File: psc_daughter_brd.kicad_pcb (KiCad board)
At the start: 2 copper layers, 30.5 x 121.9 mm, 10 parts, among them U1 AD797, U4 AD5791xRUZ, U5 BUF634AxD

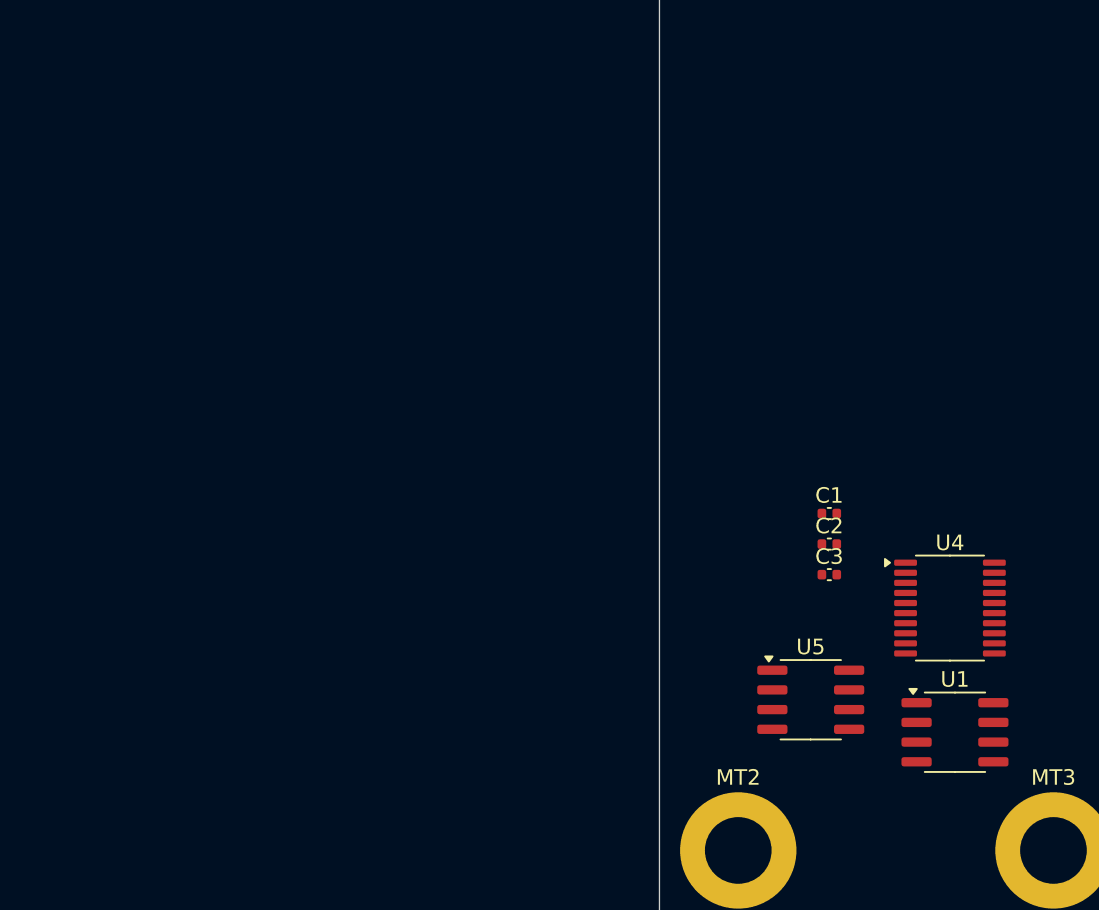
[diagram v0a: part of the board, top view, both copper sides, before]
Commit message: Add ADR1001 Voltage Reference
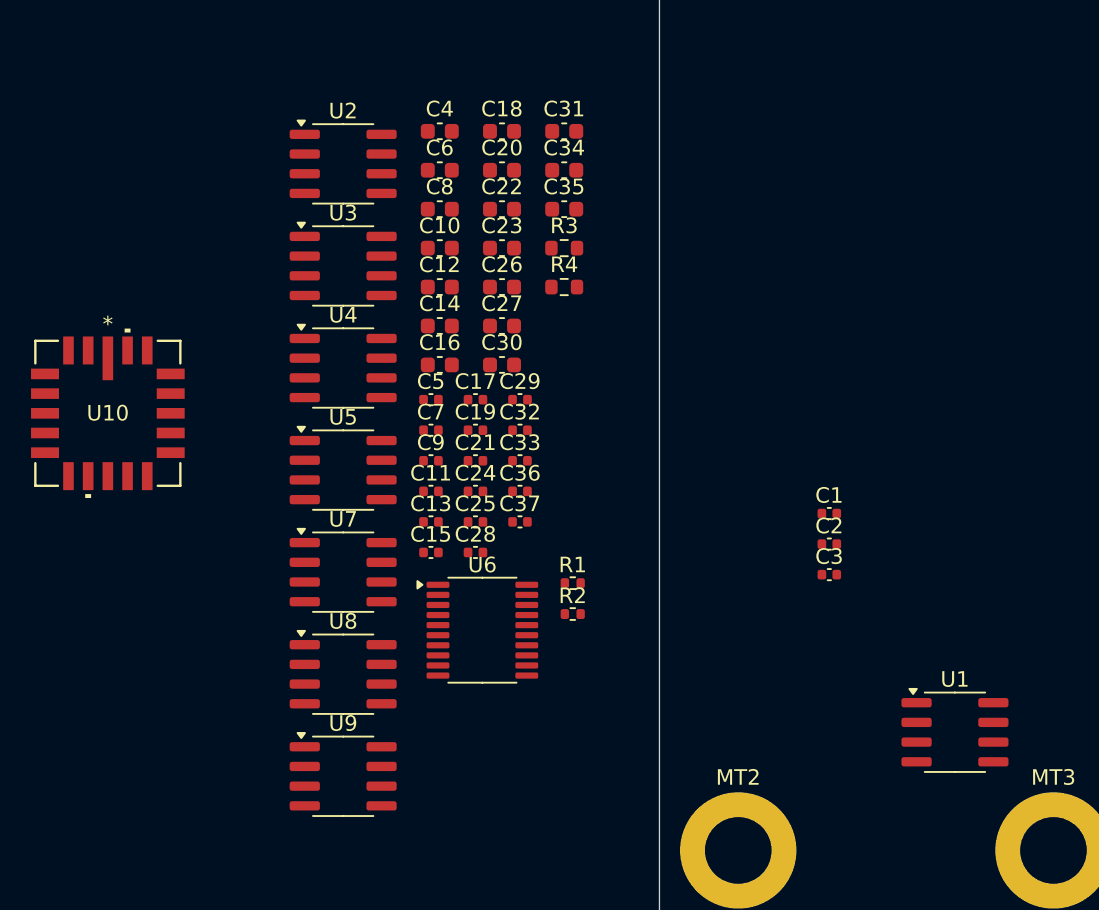
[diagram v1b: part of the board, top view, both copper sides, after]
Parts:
- added C10: 10uF, Capacitor_SMD:C_0603_1608Metric, F.Cu at (125.5, 147.9)
- added C11: 0.1uF, Capacitor_SMD:C_0402_1005Metric, F.Cu at (125.0, 163.5)
- added C12: 10uF, Capacitor_SMD:C_0603_1608Metric, F.Cu at (125.5, 150.4)
- added C13: 0.1uF, Capacitor_SMD:C_0402_1005Metric, F.Cu at (125.0, 165.5)
- added C14: 10uF, Capacitor_SMD:C_0603_1608Metric, F.Cu at (125.5, 152.9)
- added C15: 0.1uF, Capacitor_SMD:C_0402_1005Metric, F.Cu at (125.0, 167.5)
- added C16: 10uF, Capacitor_SMD:C_0603_1608Metric, F.Cu at (125.5, 155.4)
- added C17: 0.1uF, Capacitor_SMD:C_0402_1005Metric, F.Cu at (127.8, 157.6)
- added C18: 10uF, Capacitor_SMD:C_0603_1608Metric, F.Cu at (129.6, 140.3)
- added C19: 0.1uF, Capacitor_SMD:C_0402_1005Metric, F.Cu at (127.8, 159.6)
- added C20: 10uF, Capacitor_SMD:C_0603_1608Metric, F.Cu at (129.6, 142.8)
- added C21: 0.1uF, Capacitor_SMD:C_0402_1005Metric, F.Cu at (127.8, 161.6)
- added C22: 10uF, Capacitor_SMD:C_0603_1608Metric, F.Cu at (129.6, 145.3)
- added C23: 10uF, Capacitor_SMD:C_0603_1608Metric, F.Cu at (129.6, 147.9)
- added C24: 0.1uF, Capacitor_SMD:C_0402_1005Metric, F.Cu at (127.8, 163.5)
- added C25: 0.1uF, Capacitor_SMD:C_0402_1005Metric, F.Cu at (127.8, 165.5)
- added C26: 10uF, Capacitor_SMD:C_0603_1608Metric, F.Cu at (129.6, 150.4)
- added C27: 10uF, Capacitor_SMD:C_0603_1608Metric, F.Cu at (129.6, 152.9)
- added C28: 0.1uF, Capacitor_SMD:C_0402_1005Metric, F.Cu at (127.8, 167.5)
- added C29: 0.1uF, Capacitor_SMD:C_0402_1005Metric, F.Cu at (130.7, 157.6)
- added C30: 10uF, Capacitor_SMD:C_0603_1608Metric, F.Cu at (129.6, 155.4)
- added C31: 10uF, Capacitor_SMD:C_0603_1608Metric, F.Cu at (133.6, 140.3)
- added C32: 0.1uF, Capacitor_SMD:C_0402_1005Metric, F.Cu at (130.7, 159.6)
- added C33: 0.1uF, Capacitor_SMD:C_0402_1005Metric, F.Cu at (130.7, 161.6)
- added C34: 10uF, Capacitor_SMD:C_0603_1608Metric, F.Cu at (133.6, 142.8)
- added C35: 10uF, Capacitor_SMD:C_0603_1608Metric, F.Cu at (133.6, 145.3)
- added C36: 0.1uF, Capacitor_SMD:C_0402_1005Metric, F.Cu at (130.7, 163.5)
- added C37: 0.1uF, Capacitor_SMD:C_0402_1005Metric, F.Cu at (130.7, 165.5)
- added C4: 10uF, Capacitor_SMD:C_0603_1608Metric, F.Cu at (125.5, 140.3)
- added C5: 0.1uF, Capacitor_SMD:C_0402_1005Metric, F.Cu at (125.0, 157.6)
- added C6: 10uF, Capacitor_SMD:C_0603_1608Metric, F.Cu at (125.5, 142.8)
- added C7: 0.1uF, Capacitor_SMD:C_0402_1005Metric, F.Cu at (125.0, 159.6)
- added C8: 10uF, Capacitor_SMD:C_0603_1608Metric, F.Cu at (125.5, 145.3)
- added C9: 0.1uF, Capacitor_SMD:C_0402_1005Metric, F.Cu at (125.0, 161.6)
- added R1: 5.11K, Resistor_SMD:R_0402_1005Metric, F.Cu at (134.1, 169.5)
- added R2: 5.11K, Resistor_SMD:R_0402_1005Metric, F.Cu at (134.1, 171.4)
- added R3: 100, Resistor_SMD:R_0603_1608Metric, F.Cu at (133.6, 147.9)
- added R4: 100, Resistor_SMD:R_0603_1608Metric, F.Cu at (133.6, 150.4)
- added U10: ADR1001AEZ, myparts:E-20-1_ADI-M, F.Cu at (104.1, 158.5)
- added U2: AD8676xR, Package_SO:SOIC-8_3.9x4.9mm_P1.27mm, F.Cu at (119.3, 142.4)
- added U3: AD8676xR, Package_SO:SOIC-8_3.9x4.9mm_P1.27mm, F.Cu at (119.3, 149.0)
- added U6: AD5791BRUZ, Package_SO:TSSOP-20_4.4x6.5mm_P0.65mm, F.Cu at (128.3, 172.5)
- added U7: OPA277, Package_SO:SOIC-8_3.9x4.9mm_P1.27mm, F.Cu at (119.3, 168.8)
- added U8: BUF634AxD, Package_SO:SOIC-8_3.9x4.9mm_P1.27mm, F.Cu at (119.3, 175.3)
- added U9: OPA277, Package_SO:SOIC-8_3.9x4.9mm_P1.27mm, F.Cu at (119.3, 181.9)
- U4: value AD5791xRUZ -> OPA277; footprint Package_SO:TSSOP-20_4.4x6.5mm_P0.65mm -> Package_SO:SOIC-8_3.9x4.9mm_P1.27mm
- moved U4 42.1 mm to (119.3, 155.6)
- moved U5 33.6 mm to (119.3, 162.2)
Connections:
- C1 pad 1: Net-(U4-R_{FB}) -> Net-(U6-R_{FB})
- C3 pad 1: Net-(C3-Pad1) -> /DAC/dac_mon
- U1 pad 4: unconnected-(U1-V--Pad4) -> -15V
- U1 pad 6: Net-(U4-R_{FB}) -> Net-(U6-R_{FB})
- U1 pad 7: unconnected-(U1-V+-Pad7) -> +15V
- U4 pad 1: Net-(U1--) -> (no net)
- U4 pad 2: Net-(U1-+) -> /DAC/dac_mon
- U4 pad 3: unconnected-(U4-V_{REFPS}-Pad3) -> GND
- U4 pad 4: unconnected-(U4-V_{REFPF}-Pad4) -> -15V
- U4 pad 5: unconnected-(U4-V_{DD}-Pad5) -> (no net)
- U4 pad 6: unconnected-(U4-~{RESET}-Pad6) -> /DAC/dac_mon
- U4 pad 7: unconnected-(U4-~{CLR}-Pad7) -> +15V
- U4 pad 8: unconnected-(U4-~{LDAC}-Pad8) -> (no net)
- U5 pad 3: unconnected-(U5-V_{IN}-Pad3) -> Net-(U5-V_{IN})
- U5 pad 4: unconnected-(U5-V--Pad4) -> -15V
- U5 pad 6: unconnected-(U5-Pad6) -> Net-(U7--)
- U5 pad 7: unconnected-(U5-V+-Pad7) -> +15V

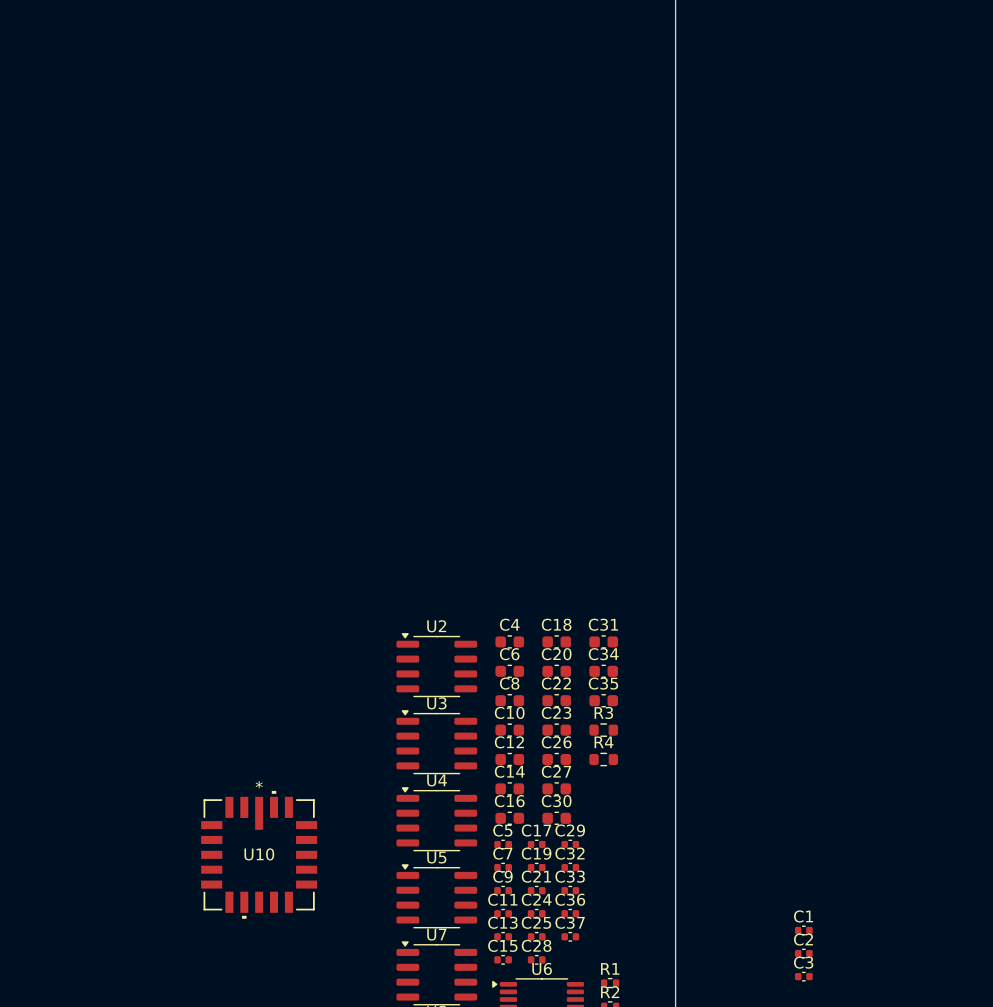
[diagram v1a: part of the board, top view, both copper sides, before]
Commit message: Add ADC monitor circuit
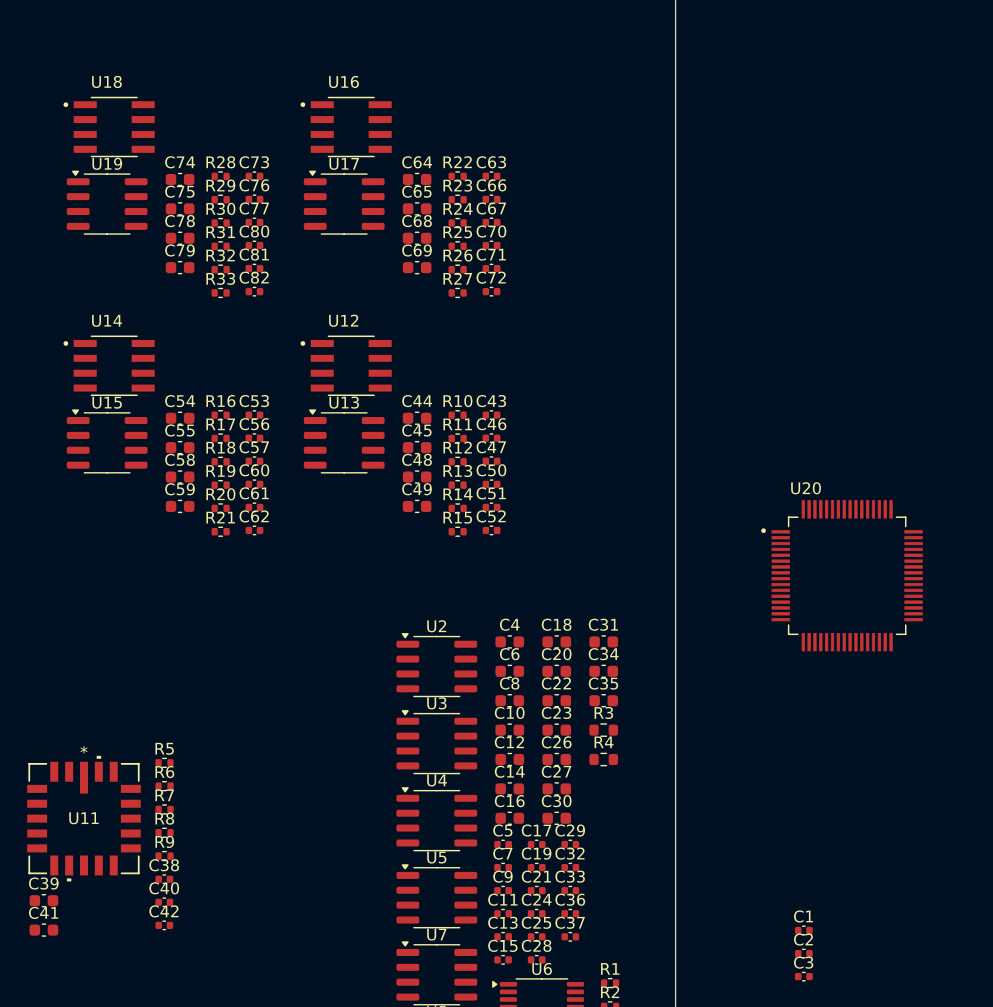
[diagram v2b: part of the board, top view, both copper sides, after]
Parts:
- removed U10: ADR1001AEZ, myparts:E-20-1_ADI-M
- added C38: 0.1uF, Capacitor_SMD:C_0402_1005Metric, F.Cu at (96.0, 160.6)
- added C39: 10uF, Capacitor_SMD:C_0603_1608Metric, F.Cu at (85.8, 162.4)
- added C40: 0.1uF, Capacitor_SMD:C_0402_1005Metric, F.Cu at (96.0, 162.6)
- added C41: 10uF, Capacitor_SMD:C_0603_1608Metric, F.Cu at (85.8, 164.9)
- added C42: 0.1uF, Capacitor_SMD:C_0402_1005Metric, F.Cu at (96.0, 164.5)
- added C43: 220pF, Capacitor_SMD:C_0402_1005Metric, F.Cu at (124.0, 121.0)
- added C44: 10uF, Capacitor_SMD:C_0603_1608Metric, F.Cu at (117.6, 121.2)
- added C45: 10uF, Capacitor_SMD:C_0603_1608Metric, F.Cu at (117.6, 123.7)
- added C46: 0.1uF, Capacitor_SMD:C_0402_1005Metric, F.Cu at (124.0, 122.9)
- added C47: 0.1uF, Capacitor_SMD:C_0402_1005Metric, F.Cu at (124.0, 124.9)
- added C48: 10uF, Capacitor_SMD:C_0603_1608Metric, F.Cu at (117.6, 126.2)
- added C49: 10uF, Capacitor_SMD:C_0603_1608Metric, F.Cu at (117.6, 128.8)
- added C50: 4700pF, Capacitor_SMD:C_0402_1005Metric, F.Cu at (124.0, 126.9)
- added C51: 0.1uF, Capacitor_SMD:C_0402_1005Metric, F.Cu at (124.0, 128.8)
- added C52: 0.1uF, Capacitor_SMD:C_0402_1005Metric, F.Cu at (124.0, 130.8)
- added C53: 220pF, Capacitor_SMD:C_0402_1005Metric, F.Cu at (103.7, 121.0)
- added C54: 10uF, Capacitor_SMD:C_0603_1608Metric, F.Cu at (97.4, 121.2)
- added C55: 10uF, Capacitor_SMD:C_0603_1608Metric, F.Cu at (97.4, 123.7)
- added C56: 0.1uF, Capacitor_SMD:C_0402_1005Metric, F.Cu at (103.7, 122.9)
- added C57: 0.1uF, Capacitor_SMD:C_0402_1005Metric, F.Cu at (103.7, 124.9)
- added C58: 10uF, Capacitor_SMD:C_0603_1608Metric, F.Cu at (97.4, 126.2)
- added C59: 10uF, Capacitor_SMD:C_0603_1608Metric, F.Cu at (97.4, 128.8)
- added C60: 4700pF, Capacitor_SMD:C_0402_1005Metric, F.Cu at (103.7, 126.9)
- added C61: 0.1uF, Capacitor_SMD:C_0402_1005Metric, F.Cu at (103.7, 128.8)
- added C62: 0.1uF, Capacitor_SMD:C_0402_1005Metric, F.Cu at (103.7, 130.8)
- added C63: 220pF, Capacitor_SMD:C_0402_1005Metric, F.Cu at (124.0, 100.6)
- added C64: 10uF, Capacitor_SMD:C_0603_1608Metric, F.Cu at (117.6, 100.8)
- added C65: 10uF, Capacitor_SMD:C_0603_1608Metric, F.Cu at (117.6, 103.3)
- added C66: 0.1uF, Capacitor_SMD:C_0402_1005Metric, F.Cu at (124.0, 102.5)
- added C67: 0.1uF, Capacitor_SMD:C_0402_1005Metric, F.Cu at (124.0, 104.5)
- added C68: 10uF, Capacitor_SMD:C_0603_1608Metric, F.Cu at (117.6, 105.9)
- added C69: 10uF, Capacitor_SMD:C_0603_1608Metric, F.Cu at (117.6, 108.4)
- added C70: 4700pF, Capacitor_SMD:C_0402_1005Metric, F.Cu at (124.0, 106.5)
- added C71: 0.1uF, Capacitor_SMD:C_0402_1005Metric, F.Cu at (124.0, 108.5)
- added C72: 0.1uF, Capacitor_SMD:C_0402_1005Metric, F.Cu at (124.0, 110.4)
- added C73: 220pF, Capacitor_SMD:C_0402_1005Metric, F.Cu at (103.7, 100.6)
- added C74: 10uF, Capacitor_SMD:C_0603_1608Metric, F.Cu at (97.4, 100.8)
- added C75: 10uF, Capacitor_SMD:C_0603_1608Metric, F.Cu at (97.4, 103.3)
- added C76: 0.1uF, Capacitor_SMD:C_0402_1005Metric, F.Cu at (103.7, 102.5)
- added C77: 0.1uF, Capacitor_SMD:C_0402_1005Metric, F.Cu at (103.7, 104.5)
- added C78: 10uF, Capacitor_SMD:C_0603_1608Metric, F.Cu at (97.4, 105.9)
- added C79: 10uF, Capacitor_SMD:C_0603_1608Metric, F.Cu at (97.4, 108.4)
- added C80: 4700pF, Capacitor_SMD:C_0402_1005Metric, F.Cu at (103.7, 106.5)
- added C81: 0.1uF, Capacitor_SMD:C_0402_1005Metric, F.Cu at (103.7, 108.5)
- added C82: 0.1uF, Capacitor_SMD:C_0402_1005Metric, F.Cu at (103.7, 110.4)
- added R10: 1K, Resistor_SMD:R_0402_1005Metric, F.Cu at (121.1, 121.0)
- added R11: 1K, Resistor_SMD:R_0402_1005Metric, F.Cu at (121.1, 123.0)
- added R12: 10, Resistor_SMD:R_0402_1005Metric, F.Cu at (121.1, 125.0)
- added R13: 10K, Resistor_SMD:R_0402_1005Metric, F.Cu at (121.1, 126.9)
- added R14: 10K, Resistor_SMD:R_0402_1005Metric, F.Cu at (121.1, 128.9)
- added R15: 10, Resistor_SMD:R_0402_1005Metric, F.Cu at (121.1, 130.9)
- added R16: 1K, Resistor_SMD:R_0402_1005Metric, F.Cu at (100.8, 121.0)
- added R17: 1K, Resistor_SMD:R_0402_1005Metric, F.Cu at (100.8, 123.0)
- added R18: 10, Resistor_SMD:R_0402_1005Metric, F.Cu at (100.8, 125.0)
- added R19: 10K, Resistor_SMD:R_0402_1005Metric, F.Cu at (100.8, 126.9)
- added R20: 10K, Resistor_SMD:R_0402_1005Metric, F.Cu at (100.8, 128.9)
- added R21: 10, Resistor_SMD:R_0402_1005Metric, F.Cu at (100.8, 130.9)
- added R22: 1K, Resistor_SMD:R_0402_1005Metric, F.Cu at (121.1, 100.6)
- added R23: 1K, Resistor_SMD:R_0402_1005Metric, F.Cu at (121.1, 102.6)
- added R24: 10, Resistor_SMD:R_0402_1005Metric, F.Cu at (121.1, 104.6)
- added R25: 10K, Resistor_SMD:R_0402_1005Metric, F.Cu at (121.1, 106.5)
- added R26: 10K, Resistor_SMD:R_0402_1005Metric, F.Cu at (121.1, 108.5)
- added R27: 10, Resistor_SMD:R_0402_1005Metric, F.Cu at (121.1, 110.5)
- added R28: 1K, Resistor_SMD:R_0402_1005Metric, F.Cu at (100.8, 100.6)
- added R29: 1K, Resistor_SMD:R_0402_1005Metric, F.Cu at (100.8, 102.6)
- added R30: 10, Resistor_SMD:R_0402_1005Metric, F.Cu at (100.8, 104.6)
- added R31: 10K, Resistor_SMD:R_0402_1005Metric, F.Cu at (100.8, 106.5)
- added R32: 10K, Resistor_SMD:R_0402_1005Metric, F.Cu at (100.8, 108.5)
- added R33: 10, Resistor_SMD:R_0402_1005Metric, F.Cu at (100.8, 110.5)
- added R5: DNP, Resistor_SMD:R_0402_1005Metric, F.Cu at (96.1, 150.7)
- added R6: 10, Resistor_SMD:R_0402_1005Metric, F.Cu at (96.1, 152.6)
- added R7: 120, Resistor_SMD:R_0402_1005Metric, F.Cu at (96.1, 154.6)
- added R8: 79K, Resistor_SMD:R_0402_1005Metric, F.Cu at (96.1, 156.6)
- added R9: 0, Resistor_SMD:R_0402_1005Metric, F.Cu at (96.1, 158.6)
- added U11: ADR1001AEZ, myparts:E-20-1_ADI, F.Cu at (89.2, 155.4)
- added U12: AD8221, myparts:SOIC127P600X175-8N, F.Cu at (112.0, 116.8)
- added U13: OPA277, Package_SO:SOIC-8_3.9x4.9mm_P1.27mm, F.Cu at (111.4, 123.3)
- added U14: AD8221, myparts:SOIC127P600X175-8N, F.Cu at (91.8, 116.8)
- added U15: OPA277, Package_SO:SOIC-8_3.9x4.9mm_P1.27mm, F.Cu at (91.2, 123.3)
- added U16: AD8221, myparts:SOIC127P600X175-8N, F.Cu at (112.0, 96.4)
- added U17: OPA277, Package_SO:SOIC-8_3.9x4.9mm_P1.27mm, F.Cu at (111.4, 102.9)
- added U18: AD8221, myparts:SOIC127P600X175-8N, F.Cu at (91.8, 96.4)
- added U19: OPA277, Package_SO:SOIC-8_3.9x4.9mm_P1.27mm, F.Cu at (91.2, 102.9)
- added U20: ADS8568SPM, myparts:QFP50P1200X1200X160-64N, F.Cu at (154.3, 134.7)
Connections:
- U2 pad 3: /DAC/10V_VREF -> /DAC/Voltage Reference/REF_OUT

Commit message: Change board size, add DB connector
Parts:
- added C83: 10uF, Capacitor_SMD:C_0603_1608Metric, F.Cu at (106.4, 59.2)
- added C84: 10uF, Capacitor_SMD:C_0603_1608Metric, F.Cu at (106.4, 61.7)
- added C85: 10uF, Capacitor_SMD:C_0603_1608Metric, F.Cu at (106.4, 64.2)
- added C86: 10uF, Capacitor_SMD:C_0603_1608Metric, F.Cu at (106.4, 66.8)
- added C87: 10uF, Capacitor_SMD:C_0603_1608Metric, F.Cu at (106.4, 69.3)
- added J1: 61082-061400LF, myparts:AMPHENOL_61082-061400LF, B.Cu at (164.7, 46.8)
- MT1, MT2, MT3, MT4: footprint MountingHole:MountingHole_4.3mm_M4_DIN965_Pad -> MountingHole:MountingHole_3.2mm_M3_Pad_TopBottom
- moved MT4 35.4 mm to (184.7, 46.8)
- moved MT1 29.4 mm to (144.7, 46.8)
- moved MT3 19.6 mm to (184.7, 186.8)
- moved MT2 0.11 mm to (144.7, 186.8)
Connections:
- U20 pad 3: unconnected-(U20-REFDN-Pad3) -> GND
- U20 pad 42: unconnected-(U20-CH_A0-Pad42) -> /Monitor/monitor_dac/mon_out
- U20 pad 43: unconnected-(U20-REFAP-Pad43) -> Net-(U20-REFAP)
- U20 pad 46: unconnected-(U20-REFAN-Pad46) -> GND
- U20 pad 49: unconnected-(U20-CH_B0-Pad49) -> /Monitor/monitor_ignd/mon_out
- U20 pad 50: unconnected-(U20-REFBP-Pad50) -> Net-(U20-REFBP)
- U20 pad 53: unconnected-(U20-REFBN-Pad53) -> GND
- U20 pad 55: unconnected-(U20-REFN-Pad55) -> GND
- U20 pad 56: unconnected-(U20-REFIO-Pad56) -> Net-(U20-REFIO)
- U20 pad 6: unconnected-(U20-REFDP-Pad6) -> Net-(U20-REFDP)
- U20 pad 60: unconnected-(U20-REFCN-Pad60) -> GND
- U20 pad 63: unconnected-(U20-REFCP-Pad63) -> Net-(U20-REFCP)
- U20 pad 64: unconnected-(U20-CH_C0-Pad64) -> /Monitor/monitor_spare/mon_out
- U20 pad 7: unconnected-(U20-CH_D0-Pad7) -> /Monitor/monitor_vout/mon_out
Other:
- board size 30.5 x 121.9 mm -> 50 x 150 mm
